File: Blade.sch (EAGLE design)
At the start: 168 parts, among them IC1 THN10-2411WIR, IC10 MCP6064-E/SL, IC12 LM78L05ACMX/NOPB, IC13 CH340G, IC2 MCP6064-E/SL, IC3 MCP6064-E/SL, IC4 MCP6064-E/SL, IC5 MAX488CSA, IC6 MOCD207MSOIC-8, IC7 MOCD207MSOIC-8, IC8 MOCD207MSOIC-8, IC9 MCP6064-E/SL, Q1 12MHz, U1 ADR366WAUJZ, U10 ADS1148QPWRQ1, U11 ADS1148QPWRQ1, U12 ADS1148QPWRQ1, U13 ADR366WAUJZ, U2 ADR366WAUJZ, U3 ADS1148QPWRQ1, U4 ADS1148QPWRQ1, U5 ADS1148QPWRQ1, U6 LT1528, U7 S70FL01GS, U8 S70FL01GS, U9 STM32F77XXXLQFP208, X1 D-SUB9-H5M09RA, X2 D-SUB15-H5M15RA, X3 USBPTH

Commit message: Widerstände Wert definiert
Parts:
- R20: value ? -> 4k7
- R21: value ? -> 470
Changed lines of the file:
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@@
 <part name="R19" library="rcl" library_urn="urn:adsk.eagle:library:334" deviceset="R-EU_" device="R0805" package3d_urn="urn:adsk.eagle:package:23553/2" value="330"/>
 <part name="LED7" library="adafruit" library_urn="urn:adsk.eagle:library:420" deviceset="LED" device="CHIP-LED0603" package3d_urn="urn:adsk.eagle:package:6240556/1"/>
-<part name="R20" library="rcl" library_urn="urn:adsk.eagle:library:334" deviceset="R-EU_" device="R0805" package3d_urn="urn:adsk.eagle:package:23553/2" value="?"/>
+<part name="R20" library="rcl" library_urn="urn:adsk.eagle:library:334" deviceset="R-EU_" device="R0805" package3d_urn="urn:adsk.eagle:package:23553/2" value="4k7"/>
 <part name="LED8" library="adafruit" library_urn="urn:adsk.eagle:library:420" deviceset="LED" device="CHIP-LED0603" package3d_urn="urn:adsk.eagle:package:6240556/1"/>
-<part name="R21" library="rcl" library_urn="urn:adsk.eagle:library:334" deviceset="R-EU_" device="R0805" package3d_urn="urn:adsk.eagle:package:23553/2" value="?"/>
+<part name="R21" library="rcl" library_urn="urn:adsk.eagle:library:334" deviceset="R-EU_" device="R0805" package3d_urn="urn:adsk.eagle:package:23553/2" value="470"/>
 <part name="X_IN_10" library="adafruit" deviceset="SMACONNECTOR" device="_EDGE"/>
 <part name="X_IN_11" library="adafruit" deviceset="SMACONNECTOR" device="_EDGE"/>

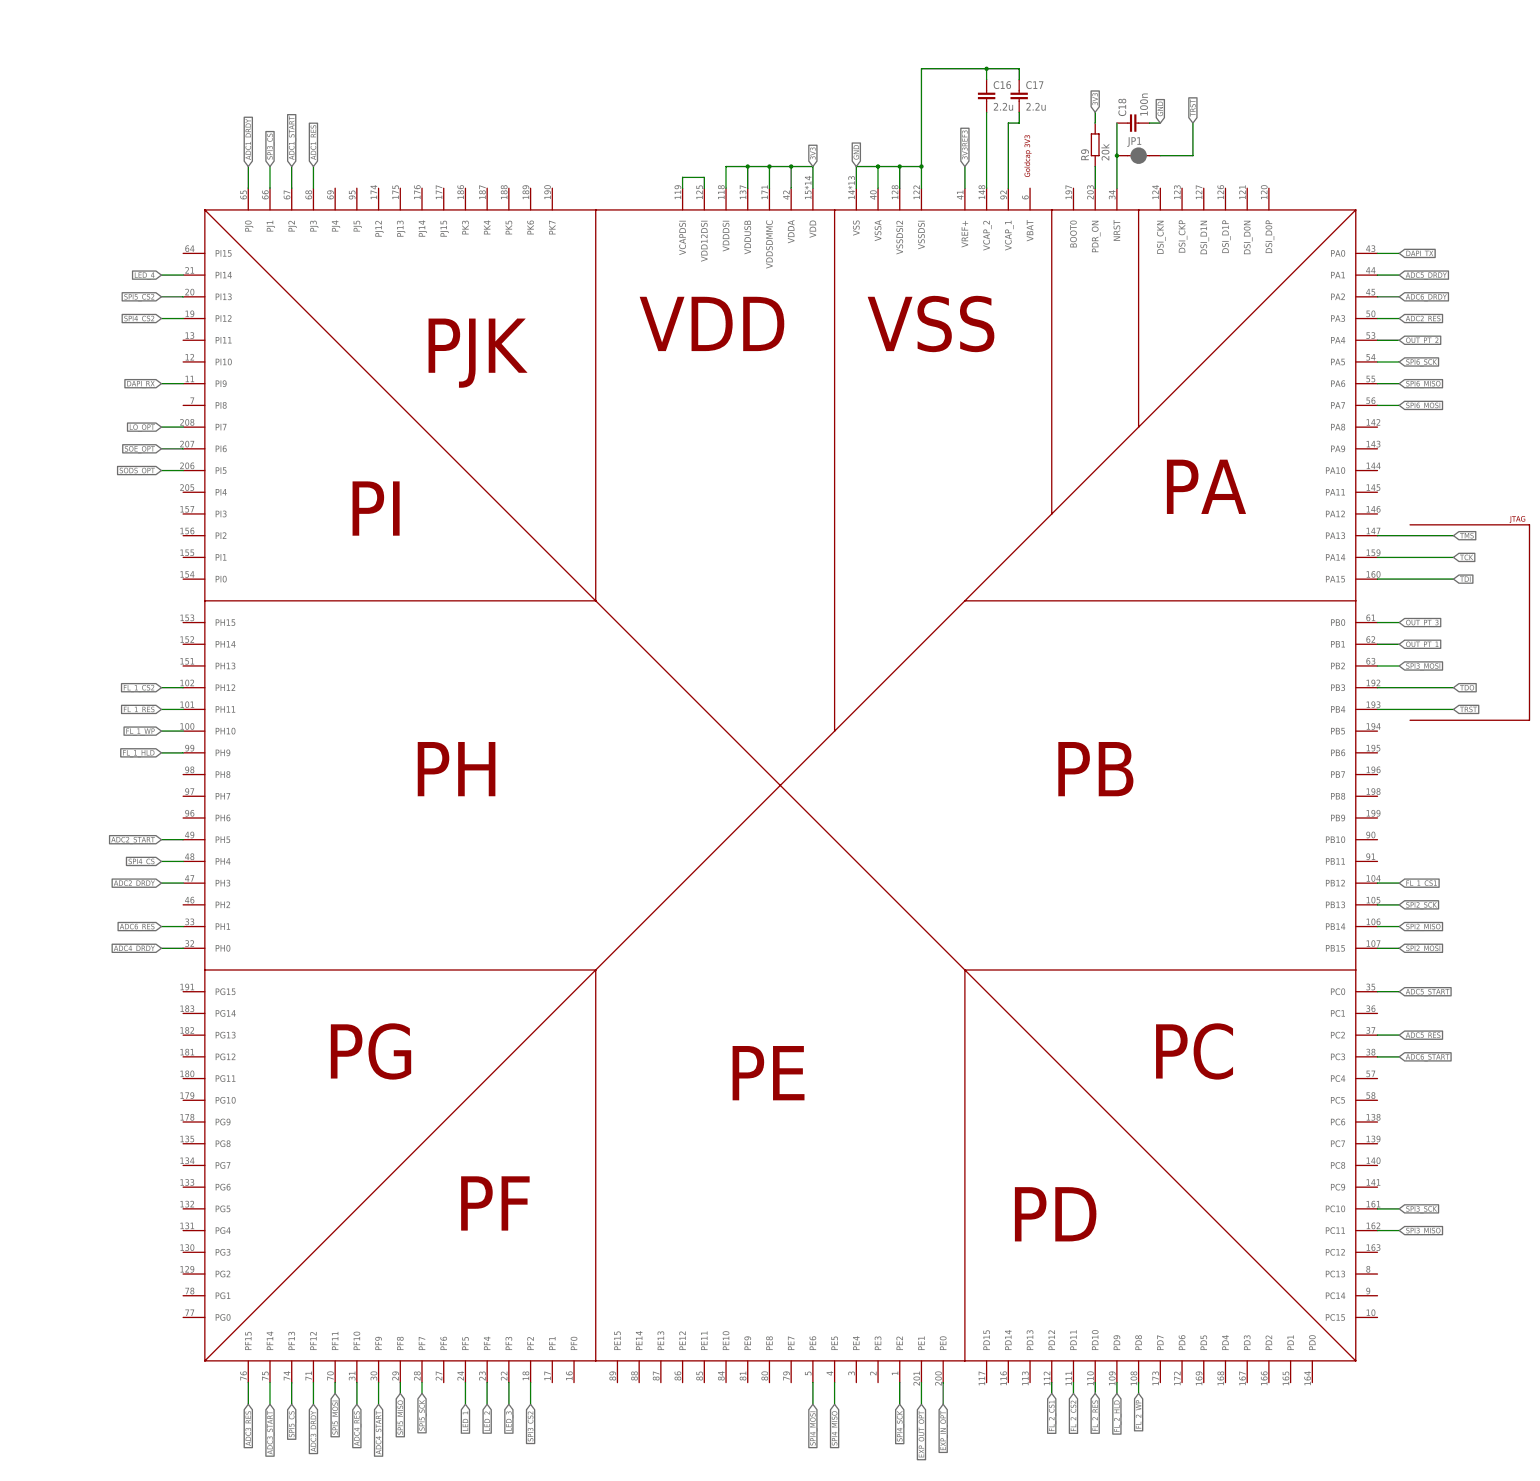
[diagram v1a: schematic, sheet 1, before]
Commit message: interspu connector, ms select
interspu connector added
master/slave (solder)jumper added
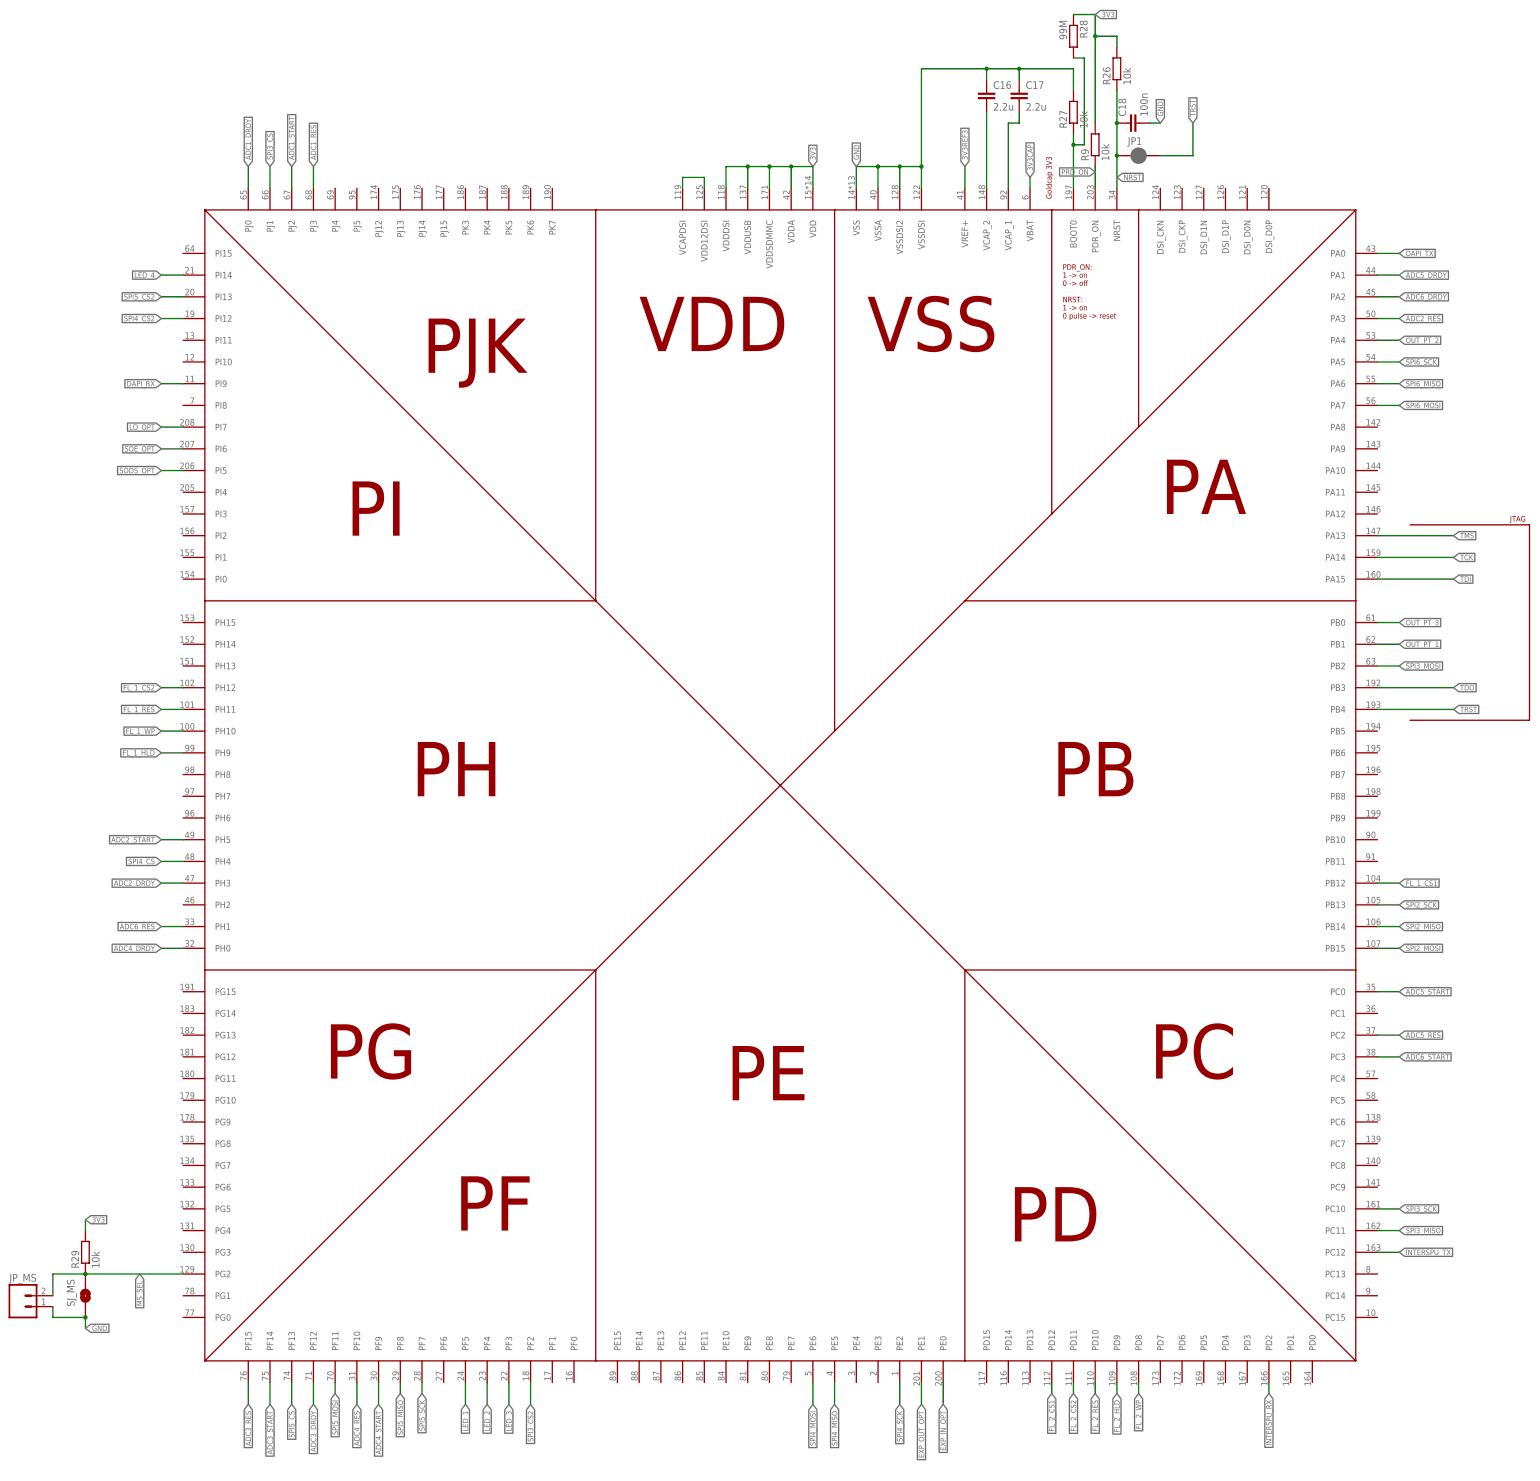
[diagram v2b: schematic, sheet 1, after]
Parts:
- added D11, D12: 3V6, diodes:DZMELF
- added JP_MS: (no value), aSparkFun:M02PTH
- added R26, R27, R29: 10k, rcl:R-EU_R0805
- added R28: 99M, rcl:R-EU_R0805
- added SJ_MS: SOLDERJUMPERNO, aSparkFun:SOLDERJUMPERNO
- D1, D2: value 3V6 -> 6V
- R12: value 3k -> 2k
- R13: value ~10k -> 4k7
- R14: value ~10k -> 7k5
- R9: value 20k -> 10k
- RN12: value 1k -> 300
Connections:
- net N$37 renamed PRD_ON
- removed net N$13: X_PROG.12
- removed net N$38: C18.1, JP1.1, U9.NRST
- removed net N$8: X_PROG.13
- new net 3V3CAP: U9.VBAT
- new net INTERSPU_RX: D11.C, U9.PD2, X1-4.F
- new net INTERSPU_TX: D12.C, U9.PC12, X1-3.F
- new net MS_SEL: JP_MS.2, R29.1, SJ_MS.2, U9.PG2
- new net N$71: R27.1, R28.2, U9.BOOT0
- new net NRST: C18.1, JP1.1, R26.1, U9.NRST
- net 3V3: now also R26.2, R28.1, R29.2; no longer X1-2.F
- net GND: now also D11.A, D12.A, JP_MS.1, R27.2, SJ_MS.1
- net LO: now also X1-7.F
- net SODS: now also X1-5.F
- net SOE: now also X1-6.F
- net TCK: no longer X1-6.F
- net TDI: no longer X1-3.F
- net TDO: now also X_PROG.13; no longer X1-5.F, X_PROG.11
- net TMS: no longer X1-7.F
- net TRST: no longer X1-4.F
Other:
- note added: "PDR_ON: 1 -> on 0 -> off NRST: 1 -> on 0 pulse -> reset"
